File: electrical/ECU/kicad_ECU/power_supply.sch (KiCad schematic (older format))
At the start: 17 parts

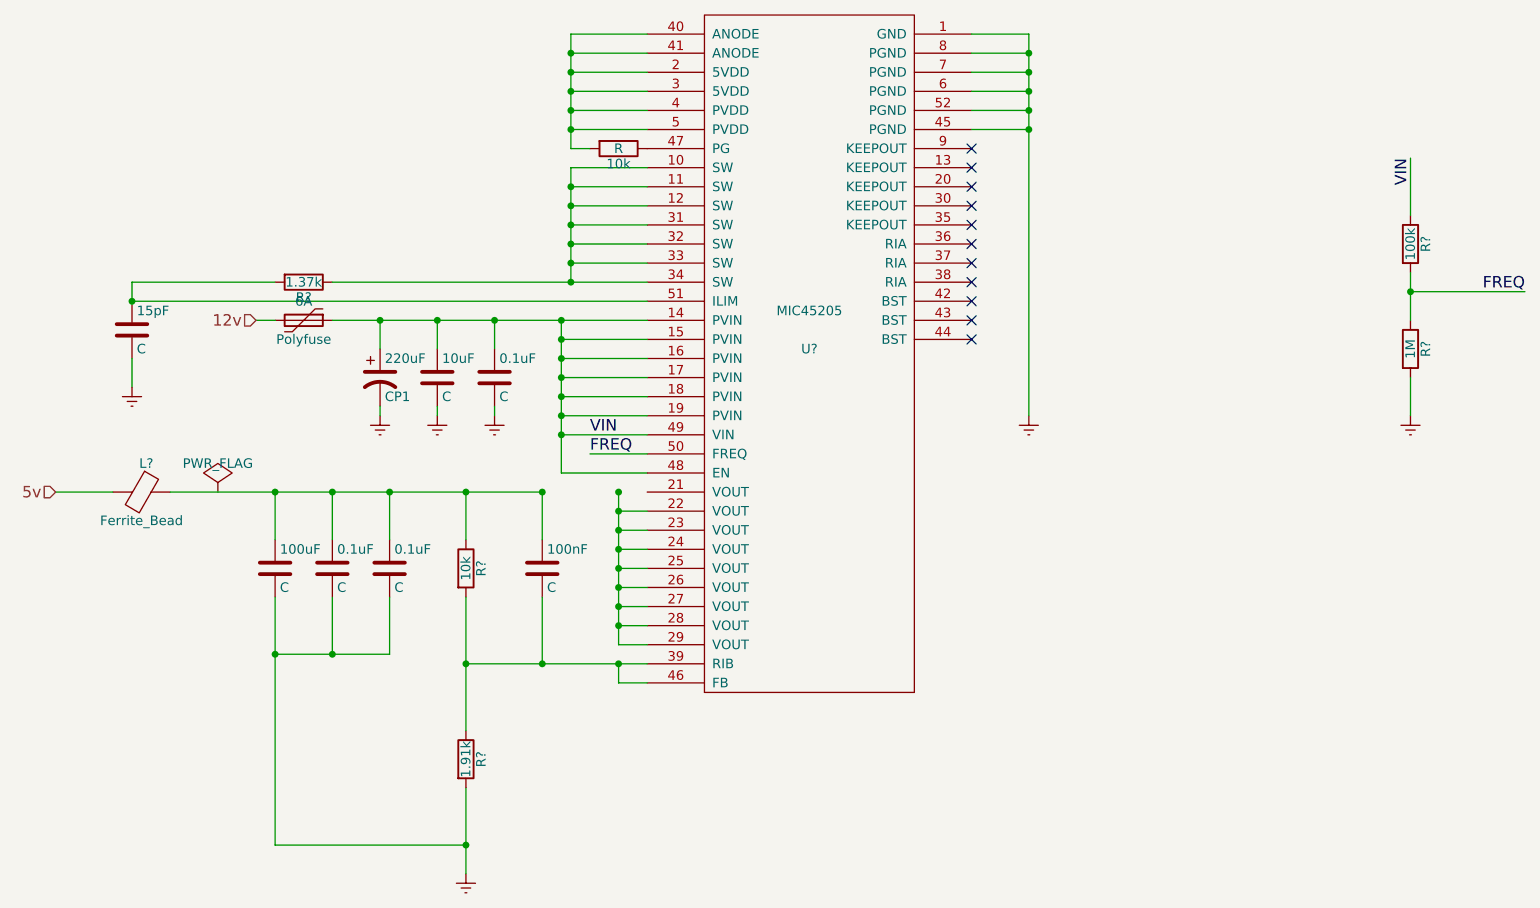
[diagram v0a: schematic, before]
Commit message: fixed some naming errors and initial round of double checking
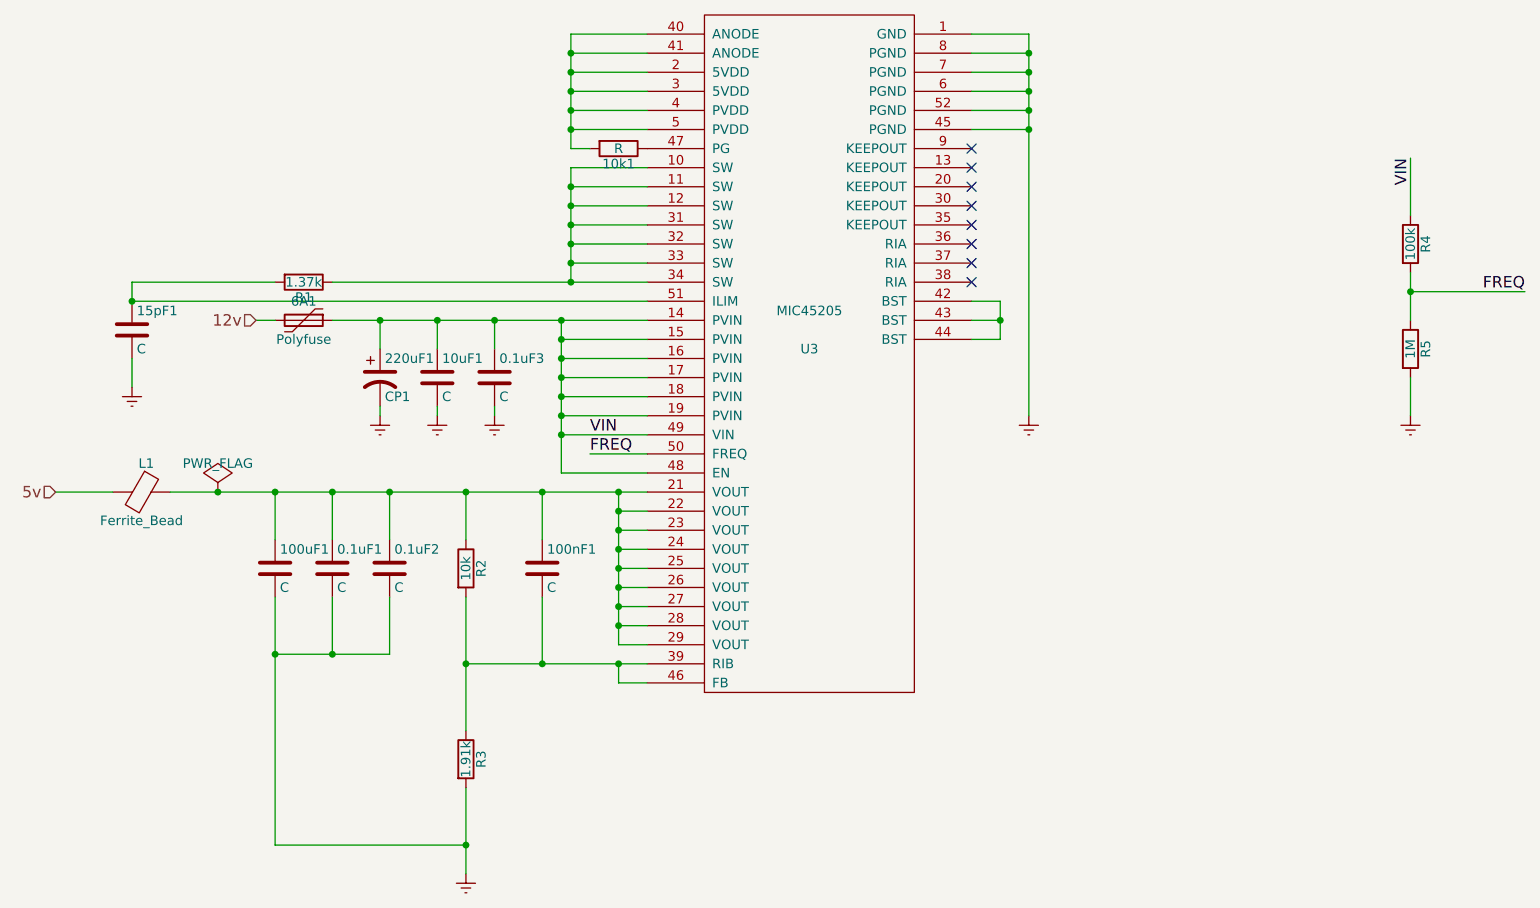
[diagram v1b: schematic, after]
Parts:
- gave numbers to parts that had none: 7
- renumbered 0.1uF to 0.1uF1, 0.1uF to 0.1uF2, 0.1uF to 0.1uF3, 100nF to 100nF1, 100uF to 100uF1, 10k to 10k1, 10uF to 10uF1, 15pF to 15pF1, 220uF to 220uF1, 6A to 6A1
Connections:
- net at U3.21 (VOUT): now also 0.1uF1.1, 0.1uF2.1, 100nF1.1, 100uF1.1, L1.1, R2.1, U3.22 (VOUT), U3.23 (VOUT), U3.24 (VOUT), U3.25 (VOUT), U3.26 (VOUT), U3.27 (VOUT), U3.28 (VOUT), U3.29 (VOUT)
- net at U3.42 (BST): now also U3.43 (BST), U3.44 (BST)
- no-connect marks 11 -> 8
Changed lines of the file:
@@
 $EndDescr
 $Comp
-L MIC45205 U?
+L MIC45205 U3
 U 1 1 597D91EA
 P 5800 3450
-F 0 "U?" H 5800 3350 50  0000 C CNN
+F 0 "U3" H 5800 3350 50  0000 C CNN
 F 1 "MIC45205" H 5800 3550 50  0000 C CNN
 F 2 "MODULE" H 5800 3450 50  0001 C CNN
@@
 NoConn ~ 6650 3100
 NoConn ~ 6650 3200
-NoConn ~ 6650 3300
-NoConn ~ 6650 3400
-NoConn ~ 6650 3500
-$Comp
-L Earth #PWR?
+$Comp
+L Earth #PWR10
 U 1 1 597DA944
 P 6950 3900
-F 0 "#PWR?" H 6950 3650 50  0001 C CNN
+F 0 "#PWR10" H 6950 3650 50  0001 C CNN
 F 1 "Earth" H 6950 3750 50  0001 C CNN
 F 2 "" H 6950 3900 50  0001 C CNN
@@
 $EndComp
 $Comp
-L R 10k
+L R 10k1
 U 1 1 597DACD4
 P 4800 2500
-F 0 "10k" V 4880 2500 50  0000 C CNN
+F 0 "10k1" V 4880 2500 50  0000 C CNN
 F 1 "R" V 4800 2500 50  0000 C CNN
 F 2 "" V 4730 2500 50  0001 C CNN
@@
 $EndComp
 $Comp
-L R R?
+L R R1
 U 1 1 597DAF82
 P 3150 3200
-F 0 "R?" V 3230 3200 50  0000 C CNN
+F 0 "R1" V 3230 3200 50  0000 C CNN
 F 1 "1.37k" V 3150 3200 50  0000 C CNN
 F 2 "" V 3080 3200 50  0001 C CNN
@@
 $EndComp
 $Comp
-L Earth #PWR?
+L Earth #PWR6
 U 1 1 597DB479
 P 3550 3900
-F 0 "#PWR?" H 3550 3650 50  0001 C CNN
+F 0 "#PWR6" H 3550 3650 50  0001 C CNN
 F 1 "Earth" H 3550 3750 50  0001 C CNN
 F 2 "" H 3550 3900 50  0001 C CNN
@@
 	3550 3850 3550 3900
 Wire Wire Line
-	2450 4300 4400 4300
+	2450 4300 4950 4300
 Wire Wire Line
 	4800 4300 4800 5100
@@
 	4500 4200 4950 4200
 $Comp
-L C 100nF
+L C 100nF1
 U 1 1 597DBD6A
 P 4400 4700
-F 0 "100nF" H 4425 4800 50  0000 L CNN
+F 0 "100nF1" H 4425 4800 50  0000 L CNN
 F 1 "C" H 4425 4600 50  0000 L CNN
 F 2 "" H 4438 4550 50  0001 C CNN
@@
 $EndComp
 $Comp
-L R R?
+L R R2
 U 1 1 597DBDE5
 P 4000 4700
-F 0 "R?" V 4080 4700 50  0000 C CNN
+F 0 "R2" V 4080 4700 50  0000 C CNN
 F 1 "10k" V 4000 4700 50  0000 C CNN
 F 2 "" V 3930 4700 50  0001 C CNN
@@
 $EndComp
 $Comp
-L R R?
+L R R3
 U 1 1 597DBE14
 P 4000 5700
-F 0 "R?" V 4080 5700 50  0000 C CNN
+F 0 "R3" V 4080 5700 50  0000 C CNN
 F 1 "1.91k" V 4000 5700 50  0000 C CNN
 F 2 "" V 3930 5700 50  0001 C CNN
@@
 $EndComp
 $Comp
-L C 100uF
+L C 100uF1
 U 1 1 597DBE45
 P 3000 4700
-F 0 "100uF" H 3025 4800 50  0000 L CNN
+F 0 "100uF1" H 3025 4800 50  0000 L CNN
 F 1 "C" H 3025 4600 50  0000 L CNN
 F 2 "" H 3038 4550 50  0001 C CNN
@@
 Connection ~ 4400 5200
 $Comp
-L Earth #PWR?
+L Earth #PWR8
 U 1 1 597DC076
 P 4000 6300
-F 0 "#PWR?" H 4000 6050 50  0001 C CNN
+F 0 "#PWR8" H 4000 6050 50  0001 C CNN
 F 1 "Earth" H 4000 6150 50  0001 C CNN
 F 2 "" H 4000 6300 50  0001 C CNN
@@
 Connection ~ 3000 4300
 $Comp
-L C 15pF
+L C 15pF1
 U 1 1 597DC6E9
 P 2250 3450
-F 0 "15pF" H 2275 3550 50  0000 L CNN
+F 0 "15pF1" H 2275 3550 50  0000 L CNN
 F 1 "C" H 2275 3350 50  0000 L CNN
 F 2 "" H 2288 3300 50  0001 C CNN
@@
 Connection ~ 2250 3300
 $Comp
-L Earth #PWR?
+L Earth #PWR5
 U 1 1 597DC726
 P 2250 3750
-F 0 "#PWR?" H 2250 3500 50  0001 C CNN
+F 0 "#PWR5" H 2250 3500 50  0001 C CNN
 F 1 "Earth" H 2250 3600 50  0001 C CNN
 F 2 "" H 2250 3750 50  0001 C CNN
@@
 	2250 3600 2250 3750
 $Comp
-L Polyfuse 6A
+L Polyfuse 6A1
 U 1 1 597DC85A
 P 3150 3400
-F 0 "6A" V 3050 3400 50  0000 C CNN
+F 0 "6A1" V 3050 3400 50  0000 C CNN
 F 1 "Polyfuse" V 3250 3400 50  0000 C CNN
 F 2 "" H 3200 3200 50  0001 L CNN
@@
 FREQ
 $Comp
-L R R?
+L R R4
 U 1 1 597DD9AA
 P 8950 3000
-F 0 "R?" V 9030 3000 50  0000 C CNN
+F 0 "R4" V 9030 3000 50  0000 C CNN
 F 1 "100k" V 8950 3000 50  0000 C CNN
 F 2 "" V 8880 3000 50  0001 C CNN
@@
 $EndComp
 $Comp
-L R R?
+L R R5
 U 1 1 597DDA07
 P 8950 3550
-F 0 "R?" V 9030 3550 50  0000 C CNN
+F 0 "R5" V 9030 3550 50  0000 C CNN
 F 1 "1M" V 8950 3550 50  0000 C CNN
 F 2 "" V 8880 3550 50  0001 C CNN
@@
 Connection ~ 8950 3250
 $Comp
-L Earth #PWR?
+L Earth #PWR11
 U 1 1 597DDBC9
 P 8950 3900
-F 0 "#PWR?" H 8950 3650 50  0001 C CNN
+F 0 "#PWR11" H 8950 3650 50  0001 C CNN
 F 1 "Earth" H 8950 3750 50  0001 C CNN
 F 2 "" H 8950 3900 50  0001 C CNN
@@
 	8950 2850 8950 2550
 $Comp
-L PWR_FLAG #FLG?
+L PWR_FLAG #FLG5
 U 1 1 597DDEFE
 P 2700 4300
-F 0 "#FLG?" H 2700 4375 50  0001 C CNN
+F 0 "#FLG5" H 2700 4375 50  0001 C CNN
 F 1 "PWR_FLAG" H 2700 4450 50  0000 C CNN
 F 2 "" H 2700 4300 50  0001 C CNN
@@
 $EndComp
 $Comp
-L C 10uF
+L C 10uF1
 U 1 1 597DE47D
 P 3850 3700
-F 0 "10uF" H 3875 3800 50  0000 L CNN
+F 0 "10uF1" H 3875 3800 50  0000 L CNN
 F 1 "C" H 3875 3600 50  0000 L CNN
 F 2 "" H 3888 3550 50  0001 C CNN
@@
 $EndComp
 $Comp
-L C 0.1uF
+L C 0.1uF3
 U 1 1 597DE4AC
 P 4150 3700
-F 0 "0.1uF" H 4175 3800 50  0000 L CNN
+F 0 "0.1uF3" H 4175 3800 50  0000 L CNN
 F 1 "C" H 4175 3600 50  0000 L CNN
 F 2 "" H 4188 3550 50  0001 C CNN
@@
 $EndComp
 $Comp
-L Earth #PWR?
+L Earth #PWR7
 U 1 1 597DE509
 P 3850 3900
-F 0 "#PWR?" H 3850 3650 50  0001 C CNN
+F 0 "#PWR7" H 3850 3650 50  0001 C CNN
 F 1 "Earth" H 3850 3750 50  0001 C CNN
 F 2 "" H 3850 3900 50  0001 C CNN
@@
 	3850 3850 3850 3900
 $Comp
-L Earth #PWR?
+L Earth #PWR9
 U 1 1 597DE53C
 P 4150 3900
-F 0 "#PWR?" H 4150 3650 50  0001 C CNN
+F 0 "#PWR9" H 4150 3650 50  0001 C CNN
 F 1 "Earth" H 4150 3750 50  0001 C CNN
 F 2 "" H 4150 3900 50  0001 C CNN
@@
 Connection ~ 4150 3400
 $Comp
-L C 0.1uF
+L C 0.1uF1
 U 1 1 597DE7F9
 P 3300 4700
-F 0 "0.1uF" H 3325 4800 50  0000 L CNN
+F 0 "0.1uF1" H 3325 4800 50  0000 L CNN
 F 1 "C" H 3325 4600 50  0000 L CNN
 F 2 "" H 3338 4550 50  0001 C CNN
@@
 $EndComp
 $Comp
-L C 0.1uF
+L C 0.1uF2
 U 1 1 597DE82E
 P 3600 4700
-F 0 "0.1uF" H 3625 4800 50  0000 L CNN
+F 0 "0.1uF2" H 3625 4800 50  0000 L CNN
 F 1 "C" H 3625 4600 50  0000 L CNN
 F 2 "" H 3638 4550 50  0001 C CNN
@@
 Connection ~ 3300 5150
 $Comp
-L CP1 220uF
+L CP1 220uF1
 U 1 1 597DEB54
 P 3550 3700
-F 0 "220uF" H 3575 3800 50  0000 L CNN
+F 0 "220uF1" H 3575 3800 50  0000 L CNN
 F 1 "CP1" H 3575 3600 50  0000 L CNN
 F 2 "" H 3550 3700 50  0001 C CNN
@@
 $EndComp
 $Comp
-L Ferrite_Bead L?
+L Ferrite_Bead L1
 U 1 1 5980C8ED
 P 2300 4300
-F 0 "L?" V 2150 4325 50  0000 C CNN
+F 0 "L1" V 2150 4325 50  0000 C CNN
 F 1 "Ferrite_Bead" V 2450 4300 50  0000 C CNN
 F 2 "" V 2230 4300 50  0001 C CNN
@@
 Wire Wire Line
 	1850 4300 2150 4300
+Connection ~ 2700 4300
+Wire Wire Line
+	6650 3300 6800 3300
+Wire Wire Line
+	6800 3300 6800 3500
+Wire Wire Line
+	6800 3500 6650 3500
+Wire Wire Line
+	6650 3400 6800 3400
+Connection ~ 6800 3400
 $EndSCHEMATC
